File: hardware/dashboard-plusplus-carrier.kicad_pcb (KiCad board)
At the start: 4 copper layers, 95 x 55 mm, 54 parts, among them J1 XT30U-M, J10a ESP32-DEVKIT-A, J10b ESP32-DEVKIT-B, J13 DEBUG, J14 TRIP + EN, J15 SPARE, J17 IGN + COOLANT, J3 TFT-ILI9488, J6 LDR + FUEL, J8 GPS_PADS, J9 HALL, Q1 IRFR9540N, U4 DPP_DCDC_MODULE

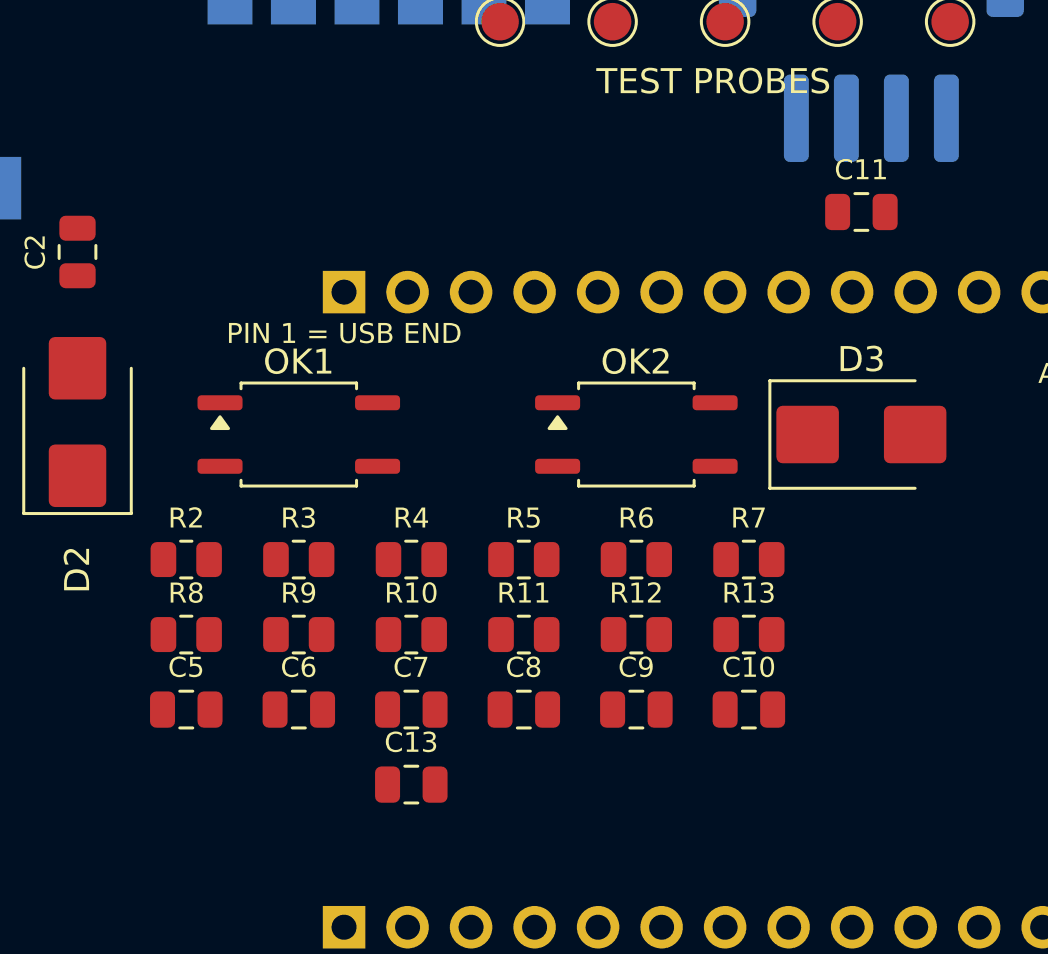
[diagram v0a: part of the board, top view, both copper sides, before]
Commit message: Open mid-band lattice to 5.40x4.34 for iron access, chain per column
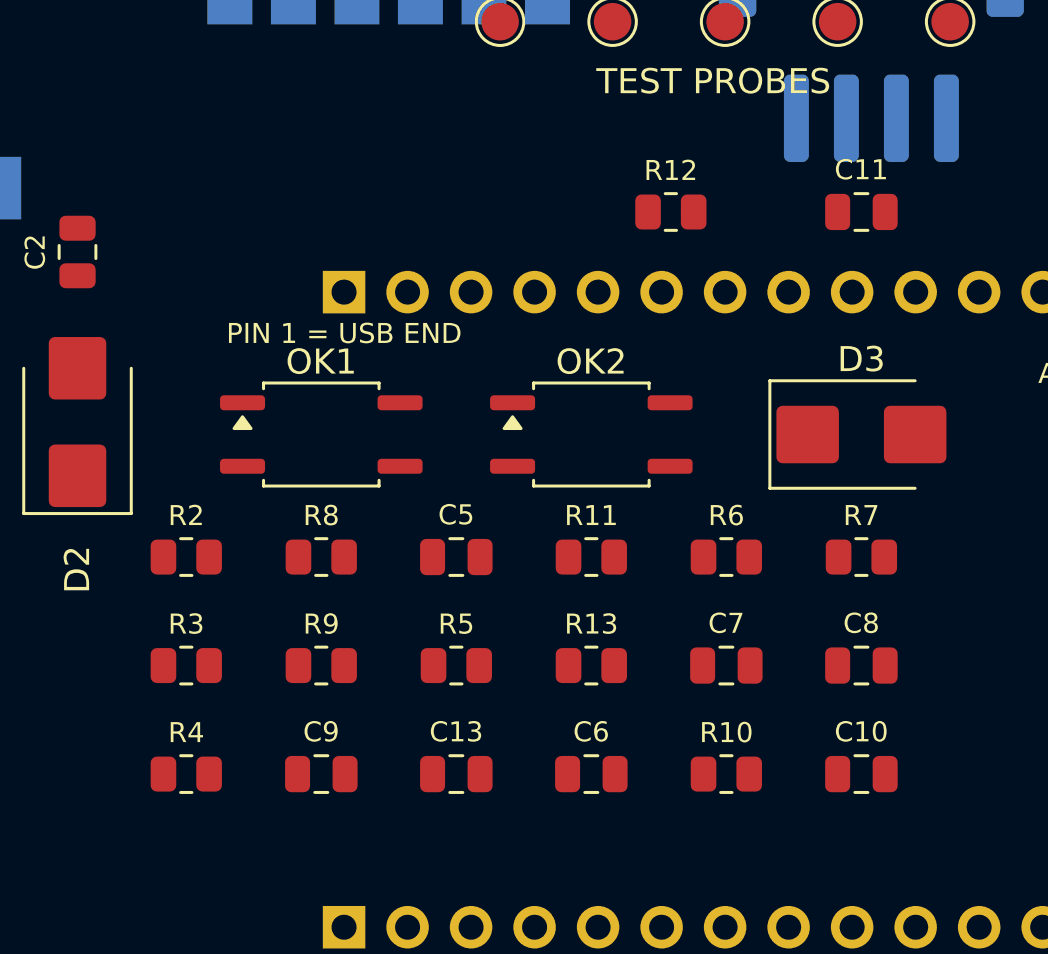
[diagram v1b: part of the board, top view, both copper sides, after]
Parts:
- removed the C10 at (163.1, 109.0)
- removed the C7 at (149.6, 109.0)
- added D3: P6SMB6V2A, dpp:D_SMB, F.Cu at (167.6, 98.0)
- added R3: 10k, dpp:R_0805_2012Metric, F.Cu at (140.6, 107.2)
- C13: renamed from R6; value 10k -> 100n; footprint dpp:R_0805_2012Metric -> dpp:C_0805_2012Metric
- C5: renamed from R4; value 1k -> 100n; footprint dpp:R_0805_2012Metric -> dpp:C_0805_2012Metric
- C6: renamed from R9; value 10k -> 100n; footprint dpp:R_0805_2012Metric -> dpp:C_0805_2012Metric
- C7: renamed from R11; value 10k -> 100n; footprint dpp:R_0805_2012Metric -> dpp:C_0805_2012Metric
- C9: renamed from R3; value 10k -> 100n; footprint dpp:R_0805_2012Metric -> dpp:C_0805_2012Metric
- OK1: renamed from C8; value 100n -> EL357N-B; footprint dpp:C_0805_2012Metric -> dpp:SO-4_4.4x3.9mm_P2.54mm
- OK2: renamed from C9; value 100n -> EL357N-B; footprint dpp:C_0805_2012Metric -> dpp:SO-4_4.4x3.9mm_P2.54mm
- R10: renamed from R12; value 10k -> 1k
- R12: renamed from D3; value P6SMB6V2A -> 10k; footprint dpp:D_SMB -> dpp:R_0805_2012Metric
- R2: renamed from C13; value 100n -> 47k; footprint dpp:C_0805_2012Metric -> dpp:R_0805_2012Metric
- R4: renamed from OK1; value EL357N-B -> 1k; footprint dpp:SO-4_4.4x3.9mm_P2.54mm -> dpp:R_0805_2012Metric
- R6: renamed from R10; value 1k -> 10k
- R7: renamed from R13; value 1k -> 10k
- R8: renamed from OK2; value EL357N-B -> 1k; footprint dpp:SO-4_4.4x3.9mm_P2.54mm -> dpp:R_0805_2012Metric
- R9: renamed from R2; value 47k -> 10k
- moved C8 27.1 mm to (167.6, 107.2)
- moved C10 22.6 mm to (167.6, 111.6)
- moved R13 16.2 mm to (156.8, 107.2)
- moved R4 14.3 mm to (140.6, 111.6)
- moved OK1 13.7 mm to (146.0, 98.0)
- moved R8 13.5 mm to (146.0, 102.9)
- moved R6 13.0 mm to (162.2, 102.9)
- moved C6 13.0 mm to (156.8, 111.6)
- moved R2 12.8 mm to (140.6, 102.9)
- moved R12 11.7 mm to (160.0, 89.1)
- moved C13 11.2 mm to (151.4, 111.6)
- moved OK2 11.1 mm to (156.8, 98.0)
- moved C9 8.63 mm to (146.0, 111.6)
- moved C7 8.19 mm to (162.2, 107.2)
- moved R9 6.87 mm to (146.0, 107.2)
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- renumbered C6 to C10, C5 to C8, R7 to R11, R8 to R13
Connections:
- C10 pad 1: FUEL_SNS -> HALL
- C13 pad 2: COOL_SNS -> GND
- C5 pad 1: BAT_DIV -> BAT_SNS
- C5 pad 2: BAT_SNS -> GND
- C6 pad 1: IGN_SENSE -> FUEL_SNS
- C7 pad 1: HALL_OUT -> COOL_SNS
- C8 pad 1: BAT_SNS -> LDR_SNS
- C9 pad 1: BAT_DIV -> IGN_SENSE
- OK1 pad 1: LDR_SNS -> IGN_LED
- OK2 pad 1: IGN_SENSE -> HALL_LED
- R10 pad 1: TFT_BL -> HALL_SIG
- R10 pad 2: GND -> HALL_LED
- R11 pad 1: V3V3 -> HALL_OUT
- R11 pad 2: LDR_SNS -> GND
- R12 pad 1: HALL -> TFT_BL
- R13 pad 1: IGN_12 -> HALL_OUT
- R13 pad 2: IGN_LED -> HALL
- R2 pad 1: V3V3 -> DC_12
- R2 pad 2: GND -> BAT_DIV
- R4 pad 1: IGN_LED -> BAT_DIV
- R4 pad 2: GND -> BAT_SNS
- R6 pad 1: HALL_SIG -> V3V3
- R6 pad 2: HALL_LED -> COOL_SNS
- R7 pad 1: HALL_OUT -> V3V3
- R7 pad 2: HALL -> LDR_SNS
- R8 pad 1: HALL_LED -> IGN_12
- R8 pad 2: GND -> IGN_LED
- R9 pad 1: DC_12 -> IGN_SENSE
- R9 pad 2: BAT_DIV -> GND

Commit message: Turn J3 180 deg to the module's pin numbering, name all 14 pads
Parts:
- moved J3 33.0 mm to (193.5, 118.5), turned to 180 degrees
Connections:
- J3 pad 1: V5 -> TFT_TPEN
- J3 pad 10: (no net) -> TFT_DC
- J3 pad 11: (no net) -> TFT_RST
- J3 pad 12: (no net) -> TFT_CS
- J3 pad 13: (no net) -> GND
- J3 pad 14: (no net) -> V5
- J3 pad 2: GND -> TFT_TDO
- J3 pad 3: TFT_CS -> TFT_TDIN
- J3 pad 4: TFT_RST -> TFT_TCS
- J3 pad 5: TFT_DC -> TFT_TCLK
- J3 pad 6: TFT_MOSI -> TFT_SDO
- J3 pad 7: TFT_SCK -> TFT_BL
- J3 pad 8: TFT_BL -> TFT_SCK
- J3 pad 9: (no net) -> TFT_MOSI
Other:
- board text added: "CS"
- board text added: "DC"
- board text added: "LED"
- board text added: "RST"
- board text added: "SCK"
- board text added: "SDI"
- board text added: "SDO"
- board text added: "TCK"
- board text added: "TCS"
- board text added: "TDI"
- board text added: "TDO"
- board text added: "TFT cont: SDO T_CLK T_CS T_DIN T_DO T_IRQ - pads 1..6 named, open"
- board text added: "TFT pad 14..1 (north to south): VCC GND CS RST DC SDI SCK LED"
- board text added: "TPN"
- board text added: "VCC"
- board text removed: "TFT 1..14: VCC GND CS RST DC SDI SCK LED SDO T_CLK T_CS"
- board text removed: "TFT cont: T_DIN TPEN T_DO"

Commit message: Put J3 back to pad 1 = VCC north, print TFT pin names flat
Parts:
- moved J3 33.0 mm to (193.5, 85.5), turned to 0 degrees
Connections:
- J3 pad 1: TFT_TPEN -> V5
- J3 pad 10: TFT_DC -> TFT_TCLK
- J3 pad 11: TFT_RST -> TFT_TCS
- J3 pad 12: TFT_CS -> TFT_TDIN
- J3 pad 13: GND -> TFT_TPEN
- J3 pad 14: V5 -> TFT_TDO
- J3 pad 2: TFT_TDO -> GND
- J3 pad 3: TFT_TDIN -> TFT_CS
- J3 pad 4: TFT_TCS -> TFT_RST
- J3 pad 5: TFT_TCLK -> TFT_DC
- J3 pad 6: TFT_SDO -> TFT_MOSI
- J3 pad 7: TFT_BL -> TFT_SCK
- J3 pad 8: TFT_SCK -> TFT_BL
- J3 pad 9: TFT_MOSI -> TFT_SDO
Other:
- board text added: "TFT 1..14: VCC GND CS RST DC SDI SCK LED SDO T_CLK T_CS"
- board text added: "TFT cont: T_DIN TPEN T_DO - pads 9..14 named, open"
- board text added: "TPEN"
- board text added: "T_CLK"
- board text added: "T_CS"
- board text added: "T_DIN"
- board text added: "T_DO"
- board text removed: "TCK"
- board text removed: "TCS"
- board text removed: "TDI"
- board text removed: "TDO"
- board text removed: "TFT cont: SDO T_CLK T_CS T_DIN T_DO T_IRQ - pads 1..6 named, open"
- board text removed: "TFT pad 14..1 (north to south): VCC GND CS RST DC SDI SCK LED"
- board text removed: "TPN"
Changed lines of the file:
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@@
 (footprint "dpp:PinSocket_1x14_P2.54mm_Vertical"
 	(layer "F.Cu")
-	(at 193.5100 118.5100 180.0)
+	(at 193.5100 85.4900 0.0)
 (descr "Through hole straight socket strip, 1x14, 2.54mm pitch, single row (from Kicad 4.0.7), script generated")
 (tags "Through hole socket strip THT 1x14 2.54mm single row")
 (property "Reference" "J3"
-		(at 0 -2.77 180)
+		(at 0 -2.77 0)
 		(layer "F.Fab")
 		(effects
@@
 	)
 (property "Value" "TFT-ILI9488"
-		(at 0 35.79 180)
+		(at 0 35.79 0)
 		(layer "F.Fab")
 		(effects
@@
 	)
 (property "KiLib_Generator" "connector/pin_header_socket"
-		(at 0 0 180)
+		(at 0 0 0)
 		(layer "F.SilkS")
 		(hide yes)
@@
 	)
 (pad "1" thru_hole rect
-		(net 33 "TFT_TPEN") (at 0 0 180)
+		(net 6 "V5") (at 0 0)
 		(size 1.7 1.7)
 		(drill 1)
@@
 	)
 (pad "2" thru_hole circle
-		(net 32 "TFT_TDO") (at 0 2.54 180)
+		(net 1 "GND") (at 0 2.54)
 		(size 1.7 1.7)
 		(drill 1)
@@
 	)
 (pad "3" thru_hole circle
-		(net 31 "TFT_TDIN") (at 0 5.08 180)
+		(net 22 "TFT_CS") (at 0 5.08)
 		(size 1.7 1.7)
 		(drill 1)
@@
 	)
 (pad "4" thru_hole circle
-		(net 30 "TFT_TCS") (at 0 7.62 180)
+		(net 26 "TFT_RST") (at 0 7.62)
 		(size 1.7 1.7)
 		(drill 1)
@@
 	)
 (pad "5" thru_hole circle
-		(net 29 "TFT_TCLK") (at 0 10.16 180)
+		(net 23 "TFT_DC") (at 0 10.16)
 		(size 1.7 1.7)
 		(drill 1)
@@
 	)
 (pad "6" thru_hole circle
-		(net 28 "TFT_SDO") (at 0 12.7 180)
+		(net 25 "TFT_MOSI") (at 0 12.7)
 		(size 1.7 1.7)
 		(drill 1)
@@
 	)
 (pad "7" thru_hole circle
-		(net 27 "TFT_BL") (at 0 15.24 180)
+		(net 24 "TFT_SCK") (at 0 15.24)
 		(size 1.7 1.7)
 		(drill 1)
@@
 	)
 (pad "8" thru_hole circle
-		(net 24 "TFT_SCK") (at 0 17.78 180)
+		(net 27 "TFT_BL") (at 0 17.78)
 		(size 1.7 1.7)
 		(drill 1)
@@
 	)
 (pad "9" thru_hole circle
-		(net 25 "TFT_MOSI") (at 0 20.32 180)
+		(net 28 "TFT_SDO") (at 0 20.32)
 		(size 1.7 1.7)
 		(drill 1)
@@
 	)
 (pad "10" thru_hole circle
-		(net 23 "TFT_DC") (at 0 22.86 180)
+		(net 29 "TFT_TCLK") (at 0 22.86)
 		(size 1.7 1.7)
 		(drill 1)
@@
 	)
 (pad "11" thru_hole circle
-		(net 26 "TFT_RST") (at 0 25.4 180)
+		(net 30 "TFT_TCS") (at 0 25.4)
 		(size 1.7 1.7)
 		(drill 1)
@@
 	)
 (pad "12" thru_hole circle
-		(net 22 "TFT_CS") (at 0 27.94 180)
+		(net 31 "TFT_TDIN") (at 0 27.94)
 		(size 1.7 1.7)
 		(drill 1)
@@
 	)
 (pad "13" thru_hole circle
-		(net 1 "GND") (at 0 30.48 180)
+		(net 33 "TFT_TPEN") (at 0 30.48)
 		(size 1.7 1.7)
 		(drill 1)
@@
 	)
 (pad "14" thru_hole circle
-		(net 6 "V5") (at 0 33.02 180)
+		(net 32 "TFT_TDO") (at 0 33.02)
 		(size 1.7 1.7)
 		(drill 1)
@@
 (gr_text "PIN 1 = USB END" (at 142.20 93.50 0.0) (layer "F.SilkS") (effects (font (size 0.80 0.80) (thickness 0.12)) (justify left top)))
 (gr_text "ANTENNA - NO COPPER" (at 174.67 95.10 0.0) (layer "F.SilkS") (effects (font (size 0.80 0.80) (thickness 0.12)) (justify left top)))
-(gr_text "TPN" (at 190.80 118.51 90.0) (layer "F.SilkS") (effects (font (size 0.80 0.80) (thickness 0.12)) (justify top)))
-(gr_text "TDO" (at 190.80 115.97 90.0) (layer "F.SilkS") (effects (font (size 0.80 0.80) (thickness 0.12)) (justify top)))
-(gr_text "TDI" (at 190.80 113.43 90.0) (layer "F.SilkS") (effects (font (size 0.80 0.80) (thickness 0.12)) (justify top)))
-(gr_text "TCS" (at 190.80 110.89 90.0) (layer "F.SilkS") (effects (font (size 0.80 0.80) (thickness 0.12)) (justify top)))
-(gr_text "TCK" (at 190.80 108.35 90.0) (layer "F.SilkS") (effects (font (size 0.80 0.80) (thickness 0.12)) (justify top)))
-(gr_text "SDO" (at 190.80 105.81 90.0) (layer "F.SilkS") (effects (font (size 0.80 0.80) (thickness 0.12)) (justify top)))
-(gr_text "LED" (at 190.80 103.27 90.0) (layer "F.SilkS") (effects (font (size 0.80 0.80) (thickness 0.12)) (justify top)))
-(gr_text "SCK" (at 190.80 100.73 90.0) (layer "F.SilkS") (effects (font (size 0.80 0.80) (thickness 0.12)) (justify top)))
-(gr_text "SDI" (at 190.80 98.19 90.0) (layer "F.SilkS") (effects (font (size 0.80 0.80) (thickness 0.12)) (justify top)))
-(gr_text "DC" (at 190.80 95.65 90.0) (layer "F.SilkS") (effects (font (size 0.80 0.80) (thickness 0.12)) (justify top)))
-(gr_text "RST" (at 190.80 93.11 90.0) (layer "F.SilkS") (effects (font (size 0.80 0.80) (thickness 0.12)) (justify top)))
-(gr_text "CS" (at 190.80 90.57 90.0) (layer "F.SilkS") (effects (font (size 0.80 0.80) (thickness 0.12)) (justify top)))
-(gr_text "GND" (at 190.80 88.03 90.0) (layer "F.SilkS") (effects (font (size 0.80 0.80) (thickness 0.12)) (justify top)))
-(gr_text "VCC" (at 190.80 85.49 90.0) (layer "F.SilkS") (effects (font (size 0.80 0.80) (thickness 0.12)) (justify top)))
-(gr_text "14" (at 188.85 85.04 0.0) (layer "F.SilkS") (effects (font (size 0.90 0.90) (thickness 0.12)) (justify left top)))
-(gr_text "1" (at 188.85 118.06 0.0) (layer "F.SilkS") (effects (font (size 0.90 0.90) (thickness 0.12)) (justify left top)))
-(gr_text "TFT" (at 189.11 103.05 90.0) (layer "F.SilkS") (effects (font (size 0.90 0.90) (thickness 0.12)) (justify left top)))
+(gr_text "VCC" (at 192.00 85.49 0.0) (layer "F.SilkS") (effects (font (size 0.80 0.80) (thickness 0.12)) (justify right)))
+(gr_text "GND" (at 192.00 88.03 0.0) (layer "F.SilkS") (effects (font (size 0.80 0.80) (thickness 0.12)) (justify right)))
+(gr_text "CS" (at 192.00 90.57 0.0) (layer "F.SilkS") (effects (font (size 0.80 0.80) (thickness 0.12)) (justify right)))
+(gr_text "RST" (at 192.00 93.11 0.0) (layer "F.SilkS") (effects (font (size 0.80 0.80) (thickness 0.12)) (justify right)))
+(gr_text "DC" (at 192.00 95.65 0.0) (layer "F.SilkS") (effects (font (size 0.80 0.80) (thickness 0.12)) (justify right)))
+(gr_text "SDI" (at 192.00 98.19 0.0) (layer "F.SilkS") (effects (font (size 0.80 0.80) (thickness 0.12)) (justify right)))
+(gr_text "SCK" (at 192.00 100.73 0.0) (layer "F.SilkS") (effects (font (size 0.80 0.80) (thickness 0.12)) (justify right)))
+(gr_text "LED" (at 192.00 103.27 0.0) (layer "F.SilkS") (effects (font (size 0.80 0.80) (thickness 0.12)) (justify right)))
+(gr_text "SDO" (at 192.00 105.81 0.0) (layer "F.SilkS") (effects (font (size 0.80 0.80) (thickness 0.12)) (justify right)))
+(gr_text "T_CLK" (at 192.00 108.35 0.0) (layer "F.SilkS") (effects (font (size 0.80 0.80) (thickness 0.12)) (justify right)))
+(gr_text "T_CS" (at 192.00 110.89 0.0) (layer "F.SilkS") (effects (font (size 0.80 0.80) (thickness 0.12)) (justify right)))
+(gr_text "T_DIN" (at 192.00 113.43 0.0) (layer "F.SilkS") (effects (font (size 0.80 0.80) (thickness 0.12)) (justify right)))
+(gr_text "TPEN" (at 192.00 115.97 0.0) (layer "F.SilkS") (effects (font (size 0.80 0.80) (thickness 0.12)) (justify right)))
+(gr_text "T_DO" (at 192.00 118.51 0.0) (layer "F.SilkS") (effects (font (size 0.80 0.80) (thickness 0.12)) (justify right)))
+(gr_text "1" (at 189.50 83.15 0.0) (layer "F.SilkS") (effects (font (size 0.90 0.90) (thickness 0.12)) (justify right)))
+(gr_text "14" (at 189.50 120.85 0.0) (layer "F.SilkS") (effects (font (size 0.90 0.90) (thickness 0.12)) (justify right)))
+(gr_text "TFT" (at 193.51 121.95 0.0) (layer "F.SilkS") (effects (font (size 0.90 0.90) (thickness 0.12)) (justify top)))
 (gr_text "+12V" (at 117.44 81.00 0.0) (layer "B.SilkS") (effects (font (size 0.90 0.90) (thickness 0.12)) (justify left top mirror)))
 (gr_text "GND" (at 133.00 81.00 0.0) (layer "B.SilkS") (effects (font (size 0.90 0.90) (thickness 0.12)) (justify left top mirror)))
@@
 (gr_text "Dashboard++ for ESP32 carrier - CAD layout rev 2 - board 95 x 55 mm" (at 111.50 133.90 0.0) (layer "Dwgs.User") (effects (font (size 1.20 1.20) (thickness 0.12)) (justify left top)))
 (gr_text "BUILD NOTES (Dwgs.User - not on the board)" (at 111.50 136.30 0.0) (layer "Dwgs.User") (effects (font (size 1.00 1.00) (thickness 0.12)) (justify left top)))
-(gr_text "TFT pad 14..1 (north to south): VCC GND CS RST DC SDI SCK LED" (at 111.50 137.90 0.0) (layer "Dwgs.User") (effects (font (size 1.00 1.00) (thickness 0.12)) (justify left top)))
-(gr_text "TFT cont: SDO T_CLK T_CS T_DIN T_DO T_IRQ - pads 1..6 named, open" (at 111.50 139.40 0.0) (layer "Dwgs.User") (effects (font (size 1.00 1.00) (thickness 0.12)) (justify left top)))
+(gr_text "TFT 1..14: VCC GND CS RST DC SDI SCK LED SDO T_CLK T_CS" (at 111.50 137.90 0.0) (layer "Dwgs.User") (effects (font (size 1.00 1.00) (thickness 0.12)) (justify left top)))
+(gr_text "TFT cont: T_DIN TPEN T_DO - pads 9..14 named, open" (at 111.50 139.40 0.0) (layer "Dwgs.User") (effects (font (size 1.00 1.00) (thickness 0.12)) (justify left top)))
 (gr_text "ESP near row 1..15 (USB end first): VIN GND 13 12 14 27 26 25" (at 111.50 140.90 0.0) (layer "Dwgs.User") (effects (font (size 1.00 1.00) (thickness 0.12)) (justify left top)))
 (gr_text "  33 32 35 34 39 36 EN" (at 111.50 142.40 0.0) (layer "Dwgs.User") (effects (font (size 1.00 1.00) (thickness 0.12)) (justify left top)))

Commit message: Move J3 VCC to the south pad, split antenna note in two
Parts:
- moved J3 33.0 mm to (193.5, 118.5), turned to 180 degrees
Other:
- board text added: "(pads 9..14 named, left open)"
- board text added: "ANTENNA"
- board text added: "NO COPPER"
- board text added: "TFT pad 1 = VCC at the SOUTH end; 1..14 north:"
- board text added: "VCC GND CS RST DC SDI SCK LED SDO T_CLK T_CS T_DIN TPEN T_DO"
- board text removed: "ANTENNA - NO COPPER"
- board text removed: "TFT 1..14: VCC GND CS RST DC SDI SCK LED SDO T_CLK T_CS"
- board text removed: "TFT cont: T_DIN TPEN T_DO - pads 9..14 named, open"
